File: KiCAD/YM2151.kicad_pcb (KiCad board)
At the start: 2 copper layers, 62.5 x 83.8 mm, 28 parts, among them J1 AudioJack3_Ground, P1 Power, P2 Analog, P3 Digital, P4 Digital, U1 YM2151, U2 YM3012, U3 LMC6484, U4 74LS04, U5 74LS00, U6 C64-Exp-Port

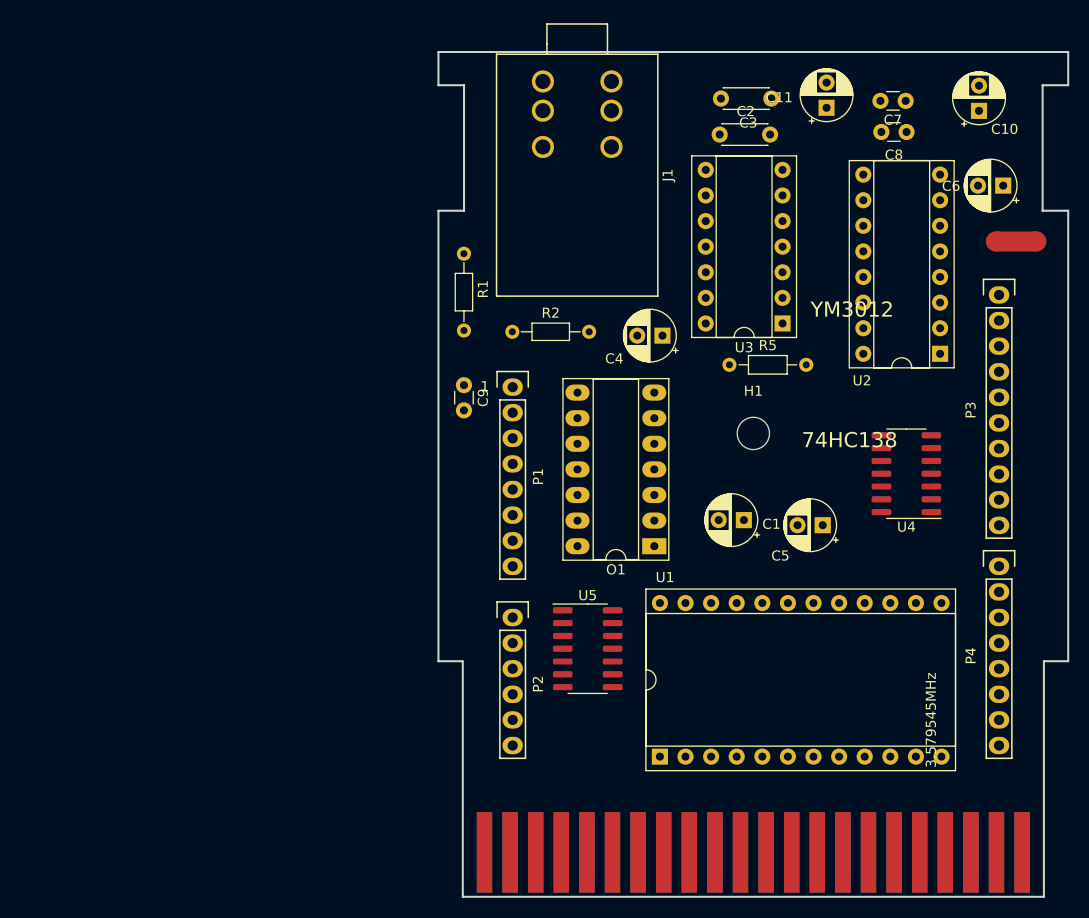
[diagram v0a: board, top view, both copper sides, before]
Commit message: microcontroller added
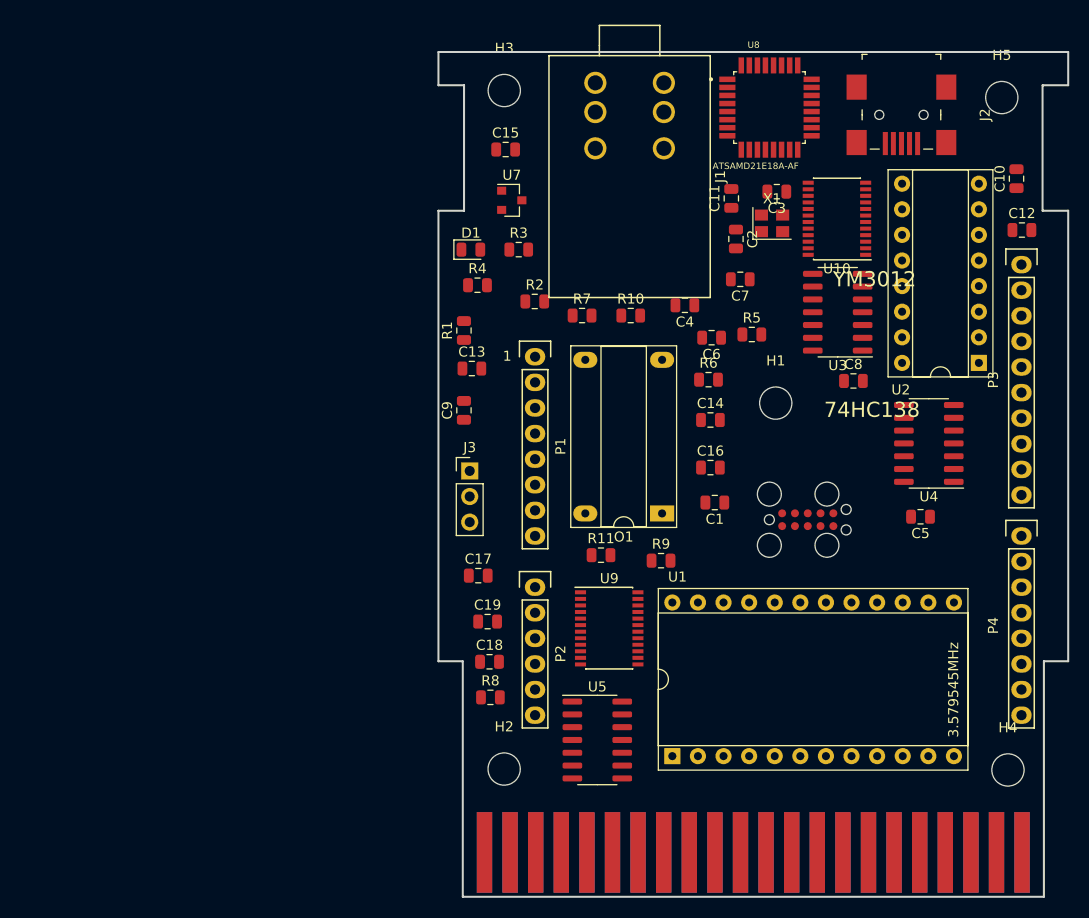
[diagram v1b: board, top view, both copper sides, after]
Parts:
- removed NT1: Net-Tie_2, NetTie:NetTie-2_SMD_Pad2.0mm
- added C12: 1uF, Capacitor_SMD:C_0805_2012Metric, F.Cu at (152.3, 58.8)
- added C13: 1uF, Capacitor_SMD:C_0805_2012Metric, F.Cu at (97.8, 72.6)
- added C14: 100nF, Capacitor_SMD:C_0805_2012Metric, F.Cu at (121.4, 77.7)
- added C15: 100nF, Capacitor_SMD:C_0805_2012Metric, F.Cu at (101.1, 50.8)
- added C16: 1uF, Capacitor_SMD:C_0805_2012Metric, F.Cu at (121.4, 82.4)
- added C17: 100nF, Capacitor_SMD:C_0805_2012Metric, F.Cu at (98.4, 93.1)
- added C18: 100nF, Capacitor_SMD:C_0805_2012Metric, F.Cu at (99.5, 101.7)
- added C19: 4.7nF/250V, Capacitor_SMD:C_0805_2012Metric, F.Cu at (99.3, 97.7)
- added D1: LED, LED_SMD:LED_0805_2012Metric, F.Cu at (97.7, 60.8)
- added H2: MountingHole, MountingHole:MountingHole_3.2mm_M3, F.Cu at (101.0, 112.3)
- added H3: MountingHole, MountingHole:MountingHole_3.2mm_M3, F.Cu at (101.0, 45.0)
- added H4: MountingHole, MountingHole:MountingHole_3.2mm_M3, F.Cu at (150.9, 112.4)
- added H5: MountingHole, MountingHole:MountingHole_3.2mm_M3, F.Cu at (150.3, 45.7)
- added J2: 690-005-299-043, KiCAD:USB_Mini_B_Female_690-005-299-043, F.Cu at (140.4, 47.4)
- added J3: Conn_01x03_Male, Connector_PinHeader_2.54mm:PinHeader_1x03_P2.54mm_Vertical, F.Cu at (97.5, 82.7)
- added P9: SWD, swd:swd, F.Cu at (131.1, 87.6)
- added R10: 10k, Resistor_SMD:R_0805_2012Metric, F.Cu at (113.5, 67.3)
- added R11: 1M, Resistor_SMD:R_0805_2012Metric, F.Cu at (110.6, 91.1)
- added R3: 10k, Resistor_SMD:R_0805_2012Metric, F.Cu at (102.4, 60.8)
- added R4: 33, Resistor_SMD:R_0805_2012Metric, F.Cu at (98.3, 64.3)
- added R6: 33, Resistor_SMD:R_0805_2012Metric, F.Cu at (121.2, 73.7)
- added R7: 10k, Resistor_SMD:R_0805_2012Metric, F.Cu at (108.7, 67.3)
- added R8: 1k, Resistor_SMD:R_0805_2012Metric, F.Cu at (99.6, 105.2)
- added R9: 10k, Resistor_SMD:R_0805_2012Metric, F.Cu at (116.5, 91.6)
- added U10: SN74AVC8T245PW, Package_SO:TSSOP-24_4.4x7.8mm_P0.65mm, F.Cu at (134.0, 57.7)
- added U7: MCP1700-3302E_SOT23, Package_TO_SOT_SMD:SOT-23, F.Cu at (101.7, 55.9)
- added U8: ATSAMD21E18A-AF, ATSAMD21E18A-AF:QFP80P900X900X120-32N, F.Cu at (127.3, 46.7)
- added U9: SN74AVC8T245PW, Package_SO:TSSOP-24_4.4x7.8mm_P0.65mm, F.Cu at (111.4, 98.4)
- added X1: ASE-xxxMHz, Oscillator:Oscillator_SMD_Abracon_ASE-4Pin_3.2x2.5mm, F.Cu at (127.5, 58.2)
- C1, C10, C11, C4, C5, C6: footprint Capacitor_THT:CP_Radial_D5.0mm_P2.50mm -> Capacitor_SMD:C_0805_2012Metric
- C2, C3: footprint Capacitor_THT:C_Disc_D4.3mm_W1.9mm_P5.00mm -> Capacitor_SMD:C_0805_2012Metric
- C7, C8, C9: footprint Capacitor_THT:C_Disc_D3.0mm_W1.6mm_P2.50mm -> Capacitor_SMD:C_0805_2012Metric
- R1, R2: footprint Resistors_THT:R_Axial_DIN0204_L3.6mm_D1.6mm_P7.62mm_Horizontal -> Resistor_SMD:R_0805_2012Metric
- R5: footprint Resistor_THT:R_Axial_DIN0204_L3.6mm_D1.6mm_P7.62mm_Horizontal -> Resistor_SMD:R_0805_2012Metric
- U3: footprint Housings_DIP:DIP-14_W7.62mm_Socket -> Package_SO:SOIC-14_3.9x8.7mm_P1.27mm
- moved C6 32.6 mm to (121.5, 69.5)
- moved C8 24.9 mm to (135.6, 73.8)
- moved C7 24.1 mm to (124.4, 63.7)
- moved C11 13.0 mm to (123.5, 55.7)
- moved C2 10.9 mm to (124.0, 59.7), turned to 270 degrees
- moved C5 9.74 mm to (142.3, 87.3)
- moved C3 9.25 mm to (128.0, 55.0)
- moved U5 9.11 mm to (110.2, 109.4)
- moved C10 7.69 mm to (151.8, 53.7)
- moved U3 5.59 mm to (134.1, 67.0)
- moved J1 5.20 mm to (113.4, 41.5)
- moved U2 3.95 mm to (148.1, 72.0)
- moved C4 3.74 mm to (118.9, 66.3)
- moved R5 3.74 mm to (125.5, 69.2)
- moved P1 3.74 mm to (104.0, 71.4)
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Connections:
- C1 pad 2: GNDA -> GND
- C10 pad 2: GNDD -> GND
- C11 pad 2: GNDD -> GND
- C2 pad 2: GNDA -> GND
- C3 pad 2: GNDA -> GND
- C6 pad 2: GNDD -> GND
- C7 pad 2: GNDD -> GND
- C8 pad 2: GNDD -> GND
- C9 pad 2: GNDD -> GND
- J1 pad S: GNDA -> GND
- O1 pad 1: Net-(O1-Pad1) -> (no net)
- O1 pad 7: GNDD -> GND
- P1 pad 6: GNDD -> GND
- P1 pad 7: GNDD -> GND
- P2 pad 1: (no net) -> /PHI2
- P2 pad 2: (no net) -> /A7
- P2 pad 3: (no net) -> /A1
- P3 pad 4: GNDD -> GND
- P3 pad 7: (no net) -> /R~W
- P3 pad 8: (no net) -> /~IO1
- U1 pad 1: GNDD -> GND
- U1 pad 11: GNDD -> GND
- U2 pad 16: GNDA -> GND
- U2 pad 3: GNDD -> GND
- U2 pad 8: GNDA -> GND
- U3 pad 11: GNDA -> GND
- U4 pad 1: GNDD -> GND
- U4 pad 11: GNDD -> GND
- U4 pad 12: (no net) -> Net-(U4-Pad12)
- U4 pad 13: GNDD -> Net-(U4-Pad13)
- U4 pad 5: /~IO2 -> /~IO1
- U4 pad 7: GNDD -> GND
- U4 pad 9: GNDD -> GND
- U5 pad 11: (no net) -> Net-(U1-Pad7)
- U5 pad 12: GNDD -> Net-(U4-Pad12)
- U5 pad 13: GNDD -> /PHI2
- U5 pad 5: /PHI2 -> /A7
- U5 pad 6: Net-(U1-Pad7) -> Net-(U4-Pad13)
- U5 pad 7: GNDD -> GND
- U6 pad 1: GNDD -> GND
- U6 pad 10: /~IO2 -> (no net)
- U6 pad 22: GNDD -> GND
- U6 pad 7: (no net) -> /~IO1
- U6 pad A: GNDD -> GND
- U6 pad R: (no net) -> /A7
- U6 pad Z: GNDD -> GND

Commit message: board routed
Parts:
- removed P2: Analog, Socket_Arduino_Uno:Socket_Strip_Arduino_1x06
- removed P3: Digital, Socket_Arduino_Uno:Socket_Strip_Arduino_1x10
- removed P4: Digital, Socket_Arduino_Uno:Socket_Strip_Arduino_1x08
- removed P9: SWD, swd:swd
- removed X1: ASE-xxxMHz, Oscillator:Oscillator_SMD_Abracon_ASE-4Pin_3.2x2.5mm
- added C20: 100n, Capacitor_SMD:C_0805_2012Metric, F.Cu at (151.6, 99.0)
- added C21: 100n, Capacitor_SMD:C_0805_2012Metric, F.Cu at (140.9, 70.1)
- added C22: 1u, Capacitor_SMD:C_0805_2012Metric, F.Cu at (122.1, 73.0)
- added C23: 10u, Capacitor_SMD:C_0805_2012Metric, F.Cu at (119.1, 73.0)
- added C24: 10u, Capacitor_SMD:C_0805_2012Metric, F.Cu at (96.1, 60.0)
- added C25: 100n, Capacitor_SMD:C_0805_2012Metric, F.Cu at (103.1, 52.7)
- added C26: 1u, Capacitor_SMD:C_0805_2012Metric, F.Cu at (107.2, 50.8)
- added C27: 10u, Capacitor_SMD:C_0805_2012Metric, F.Cu at (107.2, 53.3)
- added FB1: Ferrite_Bead, Inductor_SMD:L_1206_3216Metric, F.Cu at (118.3, 77.9)
- added FB2: Ferrite_Bead, Inductor_SMD:L_1206_3216Metric, F.Cu at (98.0, 64.7)
- added J10: IO, Connector_PinHeader_2.54mm:PinHeader_1x01_P2.54mm_Vertical, F.Cu at (153.9, 76.8)
- added J11: IO, Connector_PinHeader_2.54mm:PinHeader_1x01_P2.54mm_Vertical, F.Cu at (153.9, 74.3)
- added J12: IO, Connector_PinHeader_2.54mm:PinHeader_1x01_P2.54mm_Vertical, F.Cu at (153.9, 71.7)
- added J13: IO, Connector_PinHeader_2.54mm:PinHeader_1x01_P2.54mm_Vertical, F.Cu at (153.9, 69.2)
- added J14: IO, Connector_PinHeader_2.54mm:PinHeader_1x01_P2.54mm_Vertical, F.Cu at (153.9, 66.6)
- added J15: IO, Connector_PinHeader_2.54mm:PinHeader_1x01_P2.54mm_Vertical, F.Cu at (153.9, 64.1)
- added J16: IO, Connector_PinHeader_2.54mm:PinHeader_1x01_P2.54mm_Vertical, F.Cu at (153.9, 61.6)
- added J17: +5V, Connector_PinHeader_2.54mm:PinHeader_1x01_P2.54mm_Vertical, F.Cu at (128.5, 62.8)
- added J18: GND, Connector_PinHeader_2.54mm:PinHeader_1x01_P2.54mm_Vertical, F.Cu at (128.5, 67.9)
- added J19: +3.3V, Connector_PinHeader_2.54mm:PinHeader_1x01_P2.54mm_Vertical, F.Cu at (128.5, 57.8)
- added J4: TXI, Connector_PinHeader_2.54mm:PinHeader_1x01_P2.54mm_Vertical, F.Cu at (153.9, 92.0)
- added J5: IO, Connector_PinHeader_2.54mm:PinHeader_1x01_P2.54mm_Vertical, F.Cu at (153.9, 89.5)
- added J6: IO, Connector_PinHeader_2.54mm:PinHeader_1x01_P2.54mm_Vertical, F.Cu at (153.9, 87.0)
- added J7: IO, Connector_PinHeader_2.54mm:PinHeader_1x01_P2.54mm_Vertical, F.Cu at (153.9, 84.4)
- added J8: IO, Connector_PinHeader_2.54mm:PinHeader_1x01_P2.54mm_Vertical, F.Cu at (153.9, 81.9)
- added J9: IO, Connector_PinHeader_2.54mm:PinHeader_1x01_P2.54mm_Vertical, F.Cu at (153.9, 79.3)
- added R12: 33, Resistor_SMD:R_0805_2012Metric, F.Cu at (100.0, 79.3)
- added R13: 33, Resistor_SMD:R_0805_2012Metric, F.Cu at (104.3, 79.3)
- added R14: 33, Resistor_SMD:R_0805_2012Metric, F.Cu at (109.4, 79.3)
- added R15: 33, Resistor_SMD:R_0805_2012Metric, F.Cu at (106.9, 79.3)
- added RN1: 100k, Resistor_SMD:R_Array_Convex_8x0602, F.Cu at (143.7, 108.6)
- added RN2: 100k, Resistor_SMD:R_Array_Convex_8x0602, F.Cu at (110.0, 113.0)
- added Y1: Crystal, Crystal:Crystal_SMD_3215-2Pin_3.2x1.5mm, F.Cu at (136.7, 67.9)
- C1: value 10u -> 4.7n/250V
- C10, C11: value 4.7u -> 10u
- C12, C13: value 1uF -> 10u
- C14: value 100nF -> 10u
- C15: value 100nF -> 1uF
- C16: value 1uF -> 1u
- C17: value 100nF -> 1u
- C18: value 100nF -> 100n
- C19: value 4.7nF/250V -> 100n
- C2, C3: value 3300p -> 0.1u
- C4: value 4.7u -> 0.1u
- C5, C6: value 4.7u -> 15p
- C7: value 0.1u -> 100n
- C8, C9: value 0.1u -> 3300p
- J3: value Conn_01x03_Male -> TXO; footprint Connector_PinHeader_2.54mm:PinHeader_1x03_P2.54mm_Vertical -> Connector_PinHeader_2.54mm:PinHeader_1x01_P2.54mm_Vertical
- P1: value Power -> SWD; footprint Socket_Arduino_Uno:Socket_Strip_Arduino_1x08 -> swd:swd
- R1: value 1k -> 100
- R11: value 1M -> 10k
- R3: value 10k -> 1k
- R4: value 33 -> 10k
- R5: value 100 -> 1M
- R7: value 10k -> 33
- U1: value YM2151 -> 74LS04; footprint Housings_DIP:DIP-24_W15.24mm_Socket -> Package_SO:SOIC-14_3.9x8.7mm_P1.27mm
- U10: value SN74AVC8T245PW -> MCP1700-3302E_SOT23; footprint Package_SO:TSSOP-24_4.4x7.8mm_P0.65mm -> Package_TO_SOT_SMD:SOT-23
- U2: value YM3012 -> 74LS00; footprint Housings_DIP:DIP-16_W7.62mm_Socket -> Package_SO:SOIC-14_3.9x8.7mm_P1.27mm
- U3: value LMC6484 -> C64-Exp-Port; footprint Package_SO:SOIC-14_3.9x8.7mm_P1.27mm -> KiCAD:C64-Cart
- U4: value 74LS04 -> YM2151; footprint Package_SO:SOIC-14_3.9x8.7mm_P1.27mm -> Package_DIP:DIP-24_W15.24mm_LongPads
- U5: value 74LS00 -> YM3012; footprint Package_SO:SOIC-14_3.9x8.7mm_P1.27mm -> Package_DIP:DIP-16_W7.62mm_Socket_LongPads
- U6: value C64-Exp-Port -> LMC6484; footprint KiCAD:C64-Cart -> Package_SO:SOIC-14_3.9x8.7mm_P1.27mm
- U7: value MCP1700-3302E_SOT23 -> SN74AVC8T245PW; footprint Package_TO_SOT_SMD:SOT-23 -> Package_SO:TSSOP-24_4.4x7.8mm_P0.65mm
- U8: value ATSAMD21E18A-AF -> ATSAMD21G18A-AU; footprint ATSAMD21E18A-AF:QFP80P900X900X120-32N -> ATSAMD21G18A-AU:QFP50P900X900X120-48N
- moved U3 68.6 mm to (96.5, 124.4), turned to 0 degrees
- moved R8 68.4 mm to (144.5, 53.7), turned to 180 degrees
- moved U6 66.0 mm to (104.3, 59.0), turned to 270 degrees
- moved R4 65.7 mm to (151.3, 103.2), turned to 90 degrees
- moved C17 65.7 mm to (151.3, 54.2), turned to 180 degrees
- moved U7 63.4 mm to (145.0, 102.2), turned to 270 degrees
- moved C18 57.7 mm to (133.7, 55.2), turned to 180 degrees
- moved J3 57.5 mm to (153.9, 94.6)
- moved C2 53.9 mm to (113.9, 112.7)
- moved C10 52.7 mm to (99.2, 49.5), turned to 180 degrees
- moved C4 50.4 mm to (138.0, 113.0), turned to 90 degrees
- moved D1 49.8 mm to (146.7, 51.7), turned to 180 degrees
- moved U2 43.0 mm to (122.7, 106.7), turned to 270 degrees
- moved C13 39.1 mm to (124.0, 101.6)
- moved R10 38.9 mm to (104.0, 105.0), turned to 180 degrees
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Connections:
- C10 pad 1: VCC -> Net-(C10-Pad1)
- C10 pad 2: GND -> Net-(C10-Pad2)
- C11 pad 1: VCC -> Net-(C11-Pad1)
- C11 pad 2: GND -> Net-(C11-Pad2)
- C13 pad 1: +3V3 -> VCC
- C14 pad 1: +3V3 -> VCC
- C15 pad 1: +3V3 -> Net-(C15-Pad1)
- C16 pad 1: Net-(C16-Pad1) -> VCC
- C19 pad 1: Net-(C19-Pad1) -> +3V3
- C2 pad 1: Net-(C2-Pad1) -> VCC
- C3 pad 1: Net-(C3-Pad1) -> VCC
- C4 pad 1: Net-(C4-Pad1) -> VCC
- C4 pad 2: Net-(C4-Pad2) -> GND
- C5 pad 2: Net-(C5-Pad2) -> GND
- C6 pad 1: VCC -> Net-(C6-Pad1)
- C7 pad 1: VCC -> Net-(C22-Pad1)
- C8 pad 1: VCC -> Net-(C8-Pad1)
- C9 pad 1: VCC -> Net-(C9-Pad1)
- J2 pad 2: /SAMD21/D- -> /D-
- J2 pad 3: /SAMD21/D+ -> /D+
- J2 pad SH: Net-(C19-Pad1) -> Net-(C1-Pad1)
- P1 pad 1: (no net) -> +3V3
- P1 pad 2: (no net) -> /SWDIO
- P1 pad 3: (no net) -> GND
- P1 pad 4: (no net) -> /SWCLK
- P1 pad 6: GND -> (no net)
- P1 pad 7: GND -> (no net)
- R1 pad 1: Net-(J1-PadR) -> Net-(R1-Pad1)
- R1 pad 2: Net-(C4-Pad2) -> Net-(R1-Pad2)
- R10 pad 1: GND -> Net-(R10-Pad1)
- R10 pad 2: Net-(R10-Pad2) -> GND
- R11 pad 2: Net-(C19-Pad1) -> Net-(R11-Pad2)
- R2 pad 1: Net-(J1-PadT) -> Net-(J1-PadR)
- R2 pad 2: Net-(C5-Pad2) -> Net-(C10-Pad1)
- R3 pad 1: +3V3 -> Net-(J1-PadT)
- R3 pad 2: /SAMD21/RESET -> Net-(C11-Pad1)
- R4 pad 1: /SAMD21/D+ -> GND
- R5 pad 1: Net-(R5-Pad1) -> GND
- R5 pad 2: Net-(R5-Pad2) -> Net-(C1-Pad1)
- R6 pad 1: /SAMD21/D- -> Net-(R6-Pad1)
- R6 pad 2: Net-(R6-Pad2) -> /D-
- R7 pad 1: GND -> Net-(R7-Pad1)
- R7 pad 2: Net-(R7-Pad2) -> /D+
- R9 pad 1: Net-(R9-Pad1) -> +3V3
- R9 pad 2: GND -> /RESET
- U1 pad 10: /D0 -> (no net)
- U1 pad 12: /D1 -> Net-(U1-Pad12)
- U1 pad 13: /D2 -> Net-(U1-Pad13)
- U1 pad 14: /D3 -> VCC
- U1 pad 2: /~IRQ -> (no net)
- U1 pad 3: /~IC -> Net-(U1-Pad3)
- U1 pad 4: /A0 -> Net-(U1-Pad4)
- U1 pad 5: /R~W -> /~IO1
- U1 pad 7: Net-(U1-Pad7) -> GND
- U1 pad 9: (no net) -> GND
- U10 pad 1: +3V3 -> GND
- U10 pad 2: Net-(R10-Pad2) -> +3V3
- U10 pad 3: Net-(U10-Pad3) -> VCC
- U2 pad 1: VCC -> /A1
- U2 pad 10: Net-(C2-Pad1) -> Net-(U1-Pad6)
- U2 pad 11: Net-(R5-Pad2) -> Net-(U2-Pad11)
- U2 pad 12: Net-(U2-Pad12) -> Net-(U1-Pad12)
- U2 pad 13: Net-(U2-Pad13) -> /PHI2
- U2 pad 14: Net-(U2-Pad13) -> VCC
- U2 pad 2: Net-(U1-Pad23) -> Net-(U1-Pad4)
- U2 pad 3: GND -> Net-(U2-Pad3)
- U2 pad 4: Net-(U1-Pad21) -> Net-(U1-Pad6)
- U2 pad 5: Net-(U1-Pad19) -> /A7
- U2 pad 6: Net-(U1-Pad20) -> Net-(U1-Pad13)
- U2 pad 7: /~IC -> GND
- U2 pad 8: GND -> Net-(U1-Pad3)
- U2 pad 9: Net-(C3-Pad1) -> /R~W
- U3 pad 1: Net-(U2-Pad13) -> GND
- U3 pad 10: Net-(C2-Pad1) -> (no net)
- U3 pad 11: GND -> (no net)
- U3 pad 12: Net-(C3-Pad1) -> (no net)
- U3 pad 13: Net-(C5-Pad1) -> (no net)
- U3 pad 14: Net-(C5-Pad1) -> /D7
- U3 pad 2: Net-(U2-Pad13) -> VCC
- U3 pad 3: Net-(C1-Pad1) -> VCC
- U3 pad 4: VCC -> /~IRQ
- U3 pad 5: Net-(U2-Pad12) -> /R~W
- U3 pad 6: Net-(R5-Pad1) -> (no net)
- U3 pad 7: Net-(R5-Pad1) -> /~IO1
- U3 pad 8: Net-(C4-Pad1) -> (no net)
- U3 pad 9: Net-(C4-Pad1) -> (no net)
- U4 pad 10: (no net) -> /D0
- U4 pad 12: Net-(U4-Pad12) -> /D1
- U4 pad 13: Net-(U4-Pad13) -> /D2
- U4 pad 14: VCC -> /D3
- U4 pad 2: (no net) -> /~IRQ
- U4 pad 3: Net-(U4-Pad3) -> /~IC
- U4 pad 4: Net-(U4-Pad4) -> /A0
- U4 pad 5: /~IO1 -> /R~W
- U4 pad 6: Net-(U4-Pad6) -> Net-(U2-Pad3)
- U4 pad 7: GND -> Net-(U2-Pad11)
- U4 pad 9: GND -> (no net)
- U5 pad 1: /A1 -> Net-(C22-Pad1)
- U5 pad 10: Net-(U4-Pad6) -> Net-(C8-Pad1)
- U5 pad 11: Net-(U1-Pad7) -> Net-(R1-Pad2)
- U5 pad 12: Net-(U4-Pad12) -> Net-(U5-Pad12)
- U5 pad 13: /PHI2 -> Net-(U5-Pad13)
- U5 pad 14: VCC -> Net-(U5-Pad13)
- U5 pad 2: Net-(U4-Pad4) -> Net-(R12-Pad1)
- U5 pad 3: Net-(U1-Pad6) -> GND
- U5 pad 4: Net-(U4-Pad6) -> Net-(R13-Pad1)
- U5 pad 5: /A7 -> Net-(R15-Pad1)
- U5 pad 6: Net-(U4-Pad13) -> Net-(R14-Pad1)
- U5 pad 7: GND -> /~IC
- U5 pad 8: Net-(U4-Pad3) -> GND
- U5 pad 9: /R~W -> Net-(C9-Pad1)
- U6 pad 1: GND -> Net-(U5-Pad13)
- U6 pad 10: (no net) -> Net-(C8-Pad1)
- U6 pad 11: (no net) -> GND
- U6 pad 12: (no net) -> Net-(C9-Pad1)
- U6 pad 13: (no net) -> Net-(C11-Pad2)
- U6 pad 14: /D7 -> Net-(C11-Pad2)
- U6 pad 2: VCC -> Net-(U5-Pad13)
- U6 pad 3: VCC -> Net-(C24-Pad1)
- U6 pad 4: /~IRQ -> Net-(C25-Pad1)
- U6 pad 5: /R~W -> Net-(U5-Pad12)
- U6 pad 6: (no net) -> Net-(R1-Pad1)
- U6 pad 7: /~IO1 -> Net-(R1-Pad1)
- U6 pad 8: (no net) -> Net-(C10-Pad2)
- U6 pad 9: (no net) -> Net-(C10-Pad2)
- U7 pad 1: GND -> +3V3
- U7 pad 2: +3V3 -> Net-(R4-Pad2)
- U7 pad 3: VCC -> Net-(U7-Pad3)
- U8 pad 1: Net-(U8-Pad1) -> Net-(C5-Pad1)
- U8 pad 10: GND -> Net-(U7-Pad6)
- U8 pad 11: Net-(R7-Pad2) -> Net-(U7-Pad7)
- U8 pad 12: Net-(J3-Pad1) -> Net-(U7-Pad8)
- U8 pad 13: Net-(J3-Pad2) -> Net-(U7-Pad9)
- U8 pad 14: Net-(J3-Pad3) -> Net-(U7-Pad10)
- U8 pad 15: Net-(U8-Pad15) -> Net-(J3-Pad1)
- U8 pad 16: Net-(R10-Pad2) -> Net-(J4-Pad1)
- U8 pad 17: Net-(U10-Pad3) -> +3V3
- U8 pad 18: Net-(U10-Pad4) -> GND
- U8 pad 19: Net-(U10-Pad5) -> Net-(U8-Pad19)
- U8 pad 2: Net-(U8-Pad2) -> Net-(C6-Pad1)
- U8 pad 20: Net-(U10-Pad6) -> Net-(U8-Pad20)
- U8 pad 21: Net-(U10-Pad7) -> Net-(R4-Pad2)
- U8 pad 22: Net-(U10-Pad8) -> Net-(J5-Pad1)
- U8 pad 23: Net-(U10-Pad9) -> Net-(J6-Pad1)
- U8 pad 24: Net-(R4-Pad2) -> Net-(J7-Pad1)
- U8 pad 25: Net-(R6-Pad2) -> Net-(J8-Pad1)
- U8 pad 26: /SAMD21/RESET -> Net-(R8-Pad2)
- U8 pad 27: Net-(R8-Pad2) -> Net-(J9-Pad1)
- U8 pad 28: GND -> Net-(J10-Pad1)
- U8 pad 29: Net-(C16-Pad1) -> Net-(J11-Pad1)
- U8 pad 3: Net-(U8-Pad3) -> Net-(U7-Pad3)
- U8 pad 30: +3V3 -> Net-(J12-Pad1)
- U8 pad 31: /SAMD21/SWCLK -> Net-(J13-Pad1)
- U8 pad 32: /SAMD21/SWDIO -> Net-(J14-Pad1)
- U8 pad 4: Net-(U8-Pad4) -> Net-(U7-Pad4)
- U8 pad 5: Net-(U8-Pad5) -> GND
- U8 pad 6: Net-(U8-Pad6) -> +3V3
- U8 pad 9: +3V3 -> Net-(U7-Pad5)
- U9 pad 10: Net-(U8-Pad8) -> Net-(R10-Pad1)
- U9 pad 14: (no net) -> Net-(RN2-Pad16)
- U9 pad 15: (no net) -> /A7
- U9 pad 16: (no net) -> /A1
- U9 pad 17: (no net) -> /A0
- U9 pad 18: (no net) -> /PHI2
- U9 pad 19: (no net) -> /~IC
- U9 pad 2: Net-(R7-Pad2) -> Net-(R11-Pad2)
- U9 pad 20: (no net) -> /R~W
- U9 pad 21: (no net) -> /~IO1
- U9 pad 24: VCC -> +3V3
- U9 pad 3: Net-(U8-Pad1) -> Net-(U8-Pad48)
- U9 pad 4: Net-(U8-Pad2) -> Net-(U8-Pad7)
- U9 pad 5: Net-(U8-Pad3) -> Net-(U8-Pad8)
- U9 pad 6: Net-(U8-Pad4) -> Net-(U8-Pad19)
- U9 pad 7: Net-(U8-Pad5) -> Net-(U8-Pad20)
- U9 pad 8: Net-(U8-Pad6) -> Net-(U8-Pad37)
- U9 pad 9: Net-(U8-Pad7) -> Net-(U8-Pad38)
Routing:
- net GND: track 0.00 -> 564.7 mm, vias 0 -> 3
- net VCC: track 0.00 -> 346.7 mm, vias 0 -> 7
- net +3V3: track 0.00 -> 196.9 mm, vias 0 -> 3
- net /D1: track 0.00 -> 139.5 mm, vias 0 -> 2
- net /D0: track 0.00 -> 86.2 mm, vias 0 -> 1
- net /~IRQ: track 0.00 -> 80.8 mm
- net /A0: track 0.00 -> 80.2 mm, vias 0 -> 1
- net /~IC: track 0.00 -> 78.7 mm, vias 0 -> 1
- net /D2: track 0.00 -> 70.7 mm, vias 0 -> 2
- net /D3: track 0.00 -> 66.6 mm, vias 0 -> 1
- net Net-(U8-Pad20): track 0.00 -> 66.6 mm, vias 0 -> 2
- net /D4: track 0.00 -> 64.1 mm, vias 0 -> 1
- net Net-(U8-Pad19): track 0.00 -> 62.5 mm, vias 0 -> 2
- net /A1: track 0.00 -> 62.3 mm, vias 0 -> 2
- net Net-(U8-Pad8): track 0.00 -> 61.3 mm, vias 0 -> 2
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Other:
- net class BOLD: clearance 0.2 -> 0.2032; trace_width 0.65 -> 0.6096; via_dia 0.6 -> 0.6096; via_drill 0.4 -> 0.4064
- net class Default: clearance 0.2 -> 0.1524; trace_width 0.35 -> 0.254; via_dia 0.6 -> 0.6096; via_drill 0.4 -> 0.4064
- rule trace_clearance: 0.2 -> 0.1524
- rule trace_min: 0.2 -> 0.2032
- rule via_min_drill: 0.3 -> 0.3048
- rule via_min_size: 0.4 -> 0.508
- board text removed: "74HC138"
- board text removed: "YM3012"

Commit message: final REV A version with gerber files
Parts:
- added REF**: WEEE-Logo_4.2x6mm_SilkScreen, Symbol:WEEE-Logo_4.2x6mm_SilkScreen, F.Cu at (99.3, 104.2)
- added REF**: CE-Logo_8.5x6mm_SilkScreen, Symbol:CE-Logo_8.5x6mm_SilkScreen, F.Cu at (130.7, 73.5)
- added REF**: OSHW-Logo2_7.3x6mm_SilkScreen, Symbol:OSHW-Logo2_7.3x6mm_SilkScreen, F.Cu at (131.8, 81.7)
- moved H1 3.74 mm to (125.7, 79.0)
- moved C13 1.23 mm to (122.8, 101.9)
- moved U4 0.90 mm to (126.0, 84.0)
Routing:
- net Net-(U8-Pad19): track 62.5 -> 68.8 mm
- net Net-(R15-Pad2): track 43.9 -> 49.5 mm
- net Net-(R11-Pad2): track 54.8 -> 57.6 mm
- net Net-(R14-Pad2): track 21.9 -> 24.7 mm
- net Net-(U8-Pad38): track 57.8 -> 60.4 mm
- net /D4: track 64.1 -> 66.4 mm
- net /~IRQ: track 80.8 -> 83.1 mm
- net Net-(U8-Pad48): track 49.9 -> 52.1 mm
- net Net-(R13-Pad2): track 24.4 -> 26.4 mm
- net VCC: track 346.7 -> 348.4 mm, vias 7 -> 8
- net GND: track 564.7 -> 566.4 mm
- net /D1: track 139.5 -> 140.9 mm
- net /phM: track 6.70 -> 8.11 mm
- net /A0: track 80.2 -> 81.6 mm
- net Net-(U8-Pad37): track 60.6 -> 61.8 mm
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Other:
- board text added: "YM2151 board by Frank Buss REV A"
- board text removed: "1"
- board text removed: "3.579545MHz"

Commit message: REV B
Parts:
- removed REF**: WEEE-Logo_4.2x6mm_SilkScreen, Symbol:WEEE-Logo_4.2x6mm_SilkScreen
- removed REF**: CE-Logo_8.5x6mm_SilkScreen, Symbol:CE-Logo_8.5x6mm_SilkScreen
- removed REF**: OSHW-Logo2_7.3x6mm_SilkScreen, Symbol:OSHW-Logo2_7.3x6mm_SilkScreen
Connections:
- U9 pad 24: +3V3 -> VCC
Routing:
- net VCC: track 348.4 -> 350.6 mm
- net +3V3: track 197.2 -> 196.5 mm
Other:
- board text added: "YM2151 board by Frank Buss REV B"
- board text removed: "YM2151 board by Frank Buss REV A"
